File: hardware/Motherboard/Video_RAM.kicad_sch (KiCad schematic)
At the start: 59 parts, among them J1 DA15_Socket, J9 DIN-5_180degree, Q1 2N2222, Q2 2N2222, Q3 2N2222, Q4 2N2222, Q5 2N2222, Q6 2N2222, Q7 2N2222, U25 74LS74, U32 74LS04, U33 74LS17, U34 74LS166, U35 74LS166, U36 74LS166, U37 74LS166, U38 MK4116N, U39 MK4116N, U40 MK4116N, U41 MK4116N, U42 MK4116N, U43 MK4116N, U44 MK4116N, U45 MK4116N, U46 MK4116N, U47 MK4116N, U48 MK4116N, U49 MK4116N, U50 MK4116N, U51 MK4116N, U52 MK4116N, U53 MK4116N, U54 74LS374, U55 74LS374, U56 74LS541, U57 74LS32, U58 74LS374, U59 EF9365, U62 TBP18S030N, U63 74LS32, U64 74LS374

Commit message: WIP : passives parts, cosmetic stuffs.
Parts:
- added C43, C44, C45, C46, C47, C48, C49, C51, C52, C53, C54, C55, C56, C57, C58, C59, C60, C61, C62, C63, C64, C65, C66, C67, C68, C71: 100nF, symbol Device:C
- added R11, R5, R6: 1K, symbol Device:R
- renumbered J1 to J10
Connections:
- net TTL_B: now also R5.2
- net TTL_G: now also R6.2
- net TTL_R: now also R11.2
- net VCC12V: now also C51.1, C52.1, C53.1, C54.1
- net VCC5V: now also C43.1, C44.1, C45.1, C46.1, C47.1, C48.1, C49.1, C56.1, C58.1, C60.1, C62.1, C63.1, C64.1, C65.1, C66.1, C67.1, C68.1, C71.1, R11.1, R5.1, R6.1
- net VEE5V: now also C55.2, C57.2, C59.2, C61.2
- net VSS: now also C43.2, C44.2, C45.2, C46.2, C47.2, C48.2, C49.2, C51.2, C52.2, C53.2, C54.2, C55.1, C56.2, C57.1, C58.2, C59.1, C60.2, C61.1, C62.2, C63.2, C64.2, C65.2, C66.2, C67.2, C68.2, C71.2
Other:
- moved on the sheet: U32G, U33G, U57E, U63E

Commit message: Footprints.
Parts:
- C43, C44, C45, C46, C47, C48, C49, C51, C52, C53, C54, C55, C56, C57, C58, C59, C60, C61, C62, C63, C64, C65, C66, C67, C68, C71: footprint (none) -> Capacitor_THT:C_Disc_D9.0mm_W2.5mm_P5.00mm
- J10: footprint (none) -> Connector_Dsub:DSUB-15_Socket_Horizontal_P2.77x2.84mm_EdgePinOffset9.40mm
- J9: footprint (none) -> Connector_PinHeader_2.54mm:PinHeader_1x05_P2.54mm_Vertical
- R1, R10, R11, R12, R13, R14, R15, R16, R17, R18, R19, R2, R3, R4, R41, R46, R5, R6, R7, R8, R9: footprint (none) -> Resistor_THT:R_Axial_DIN0309_L9.0mm_D3.2mm_P12.70mm_Horizontal
- U25, U32, U33, U57, U63: footprint (none) -> Package_DIP:DIP-14_W7.62mm_Socket
- U34, U35, U36, U37, U62: footprint (none) -> Package_DIP:DIP-16_W7.62mm_Socket
- U38, U39, U40, U41, U42, U43, U44, U45, U46, U47, U48, U49, U50, U51, U52, U53: footprint Package_DIP:DIP-16_W7.62mm -> Package_DIP:DIP-16_W7.62mm_Socket
- U54, U55, U56, U58, U64: footprint (none) -> Package_DIP:DIP-20_W7.62mm_Socket
- U59: footprint Package_DIP:DIP-40_W15.24mm -> Package_DIP:DIP-40_W15.24mm_Socket

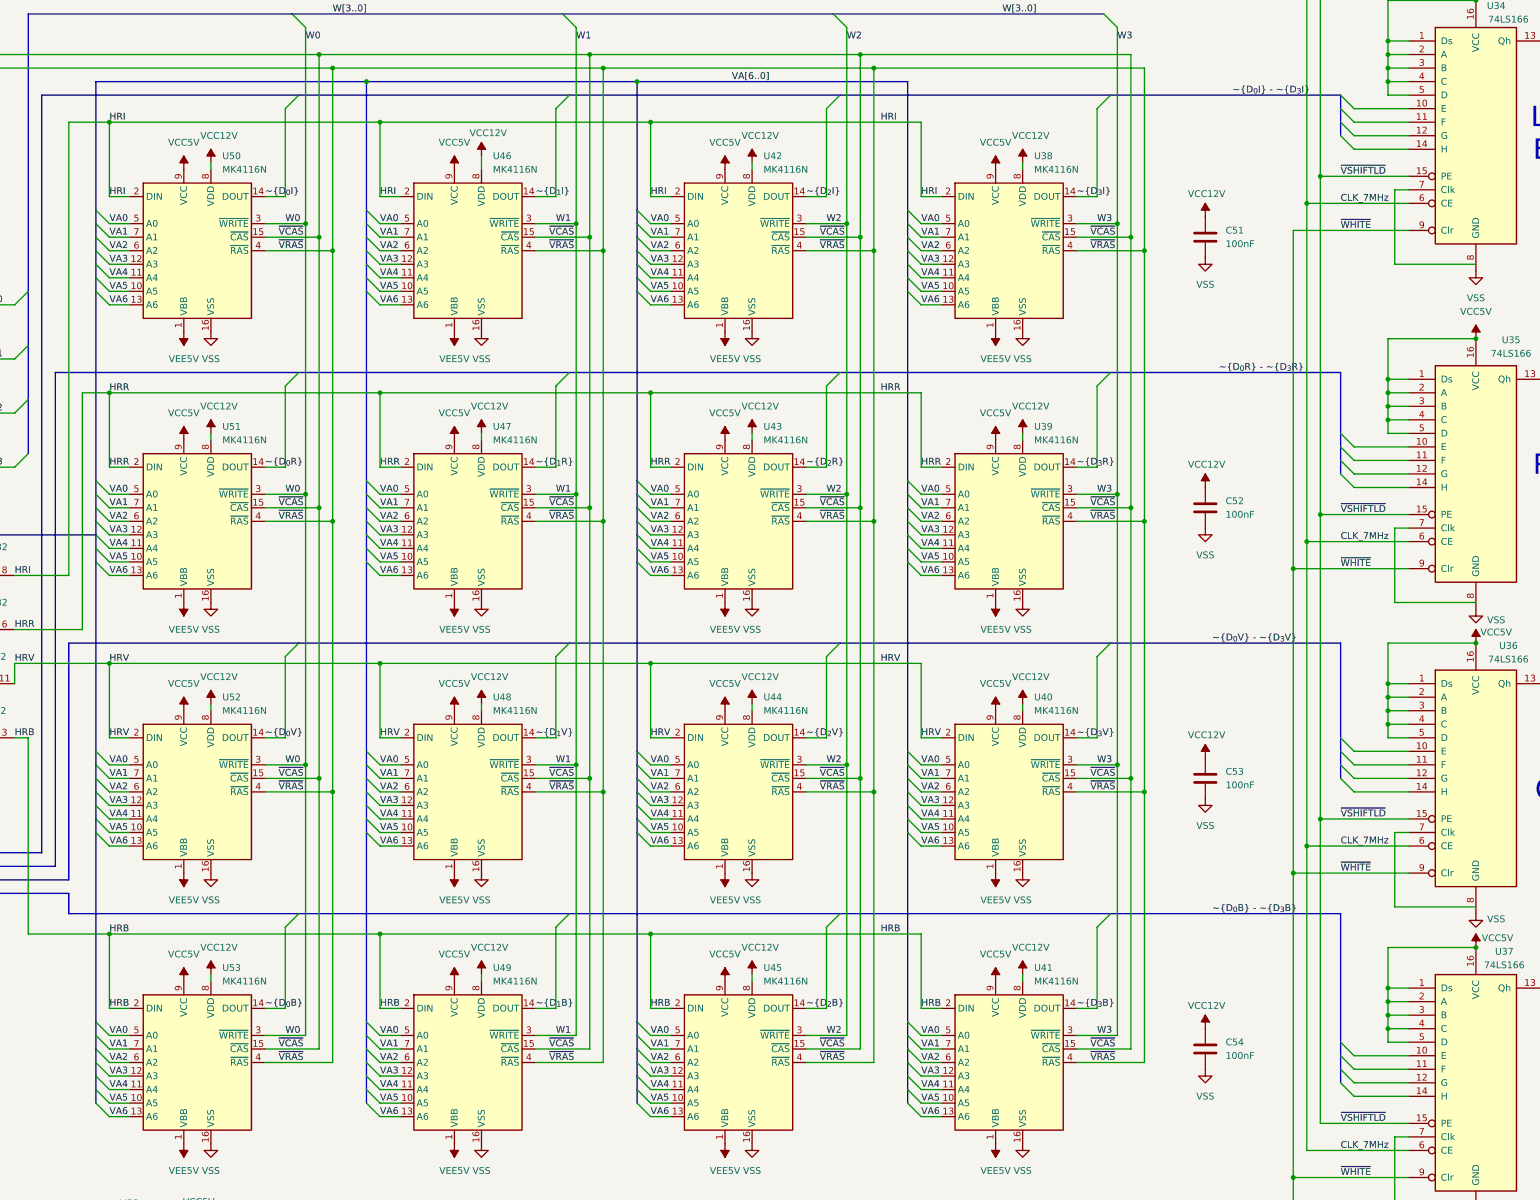
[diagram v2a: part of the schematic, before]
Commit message: fix dram address bit order.
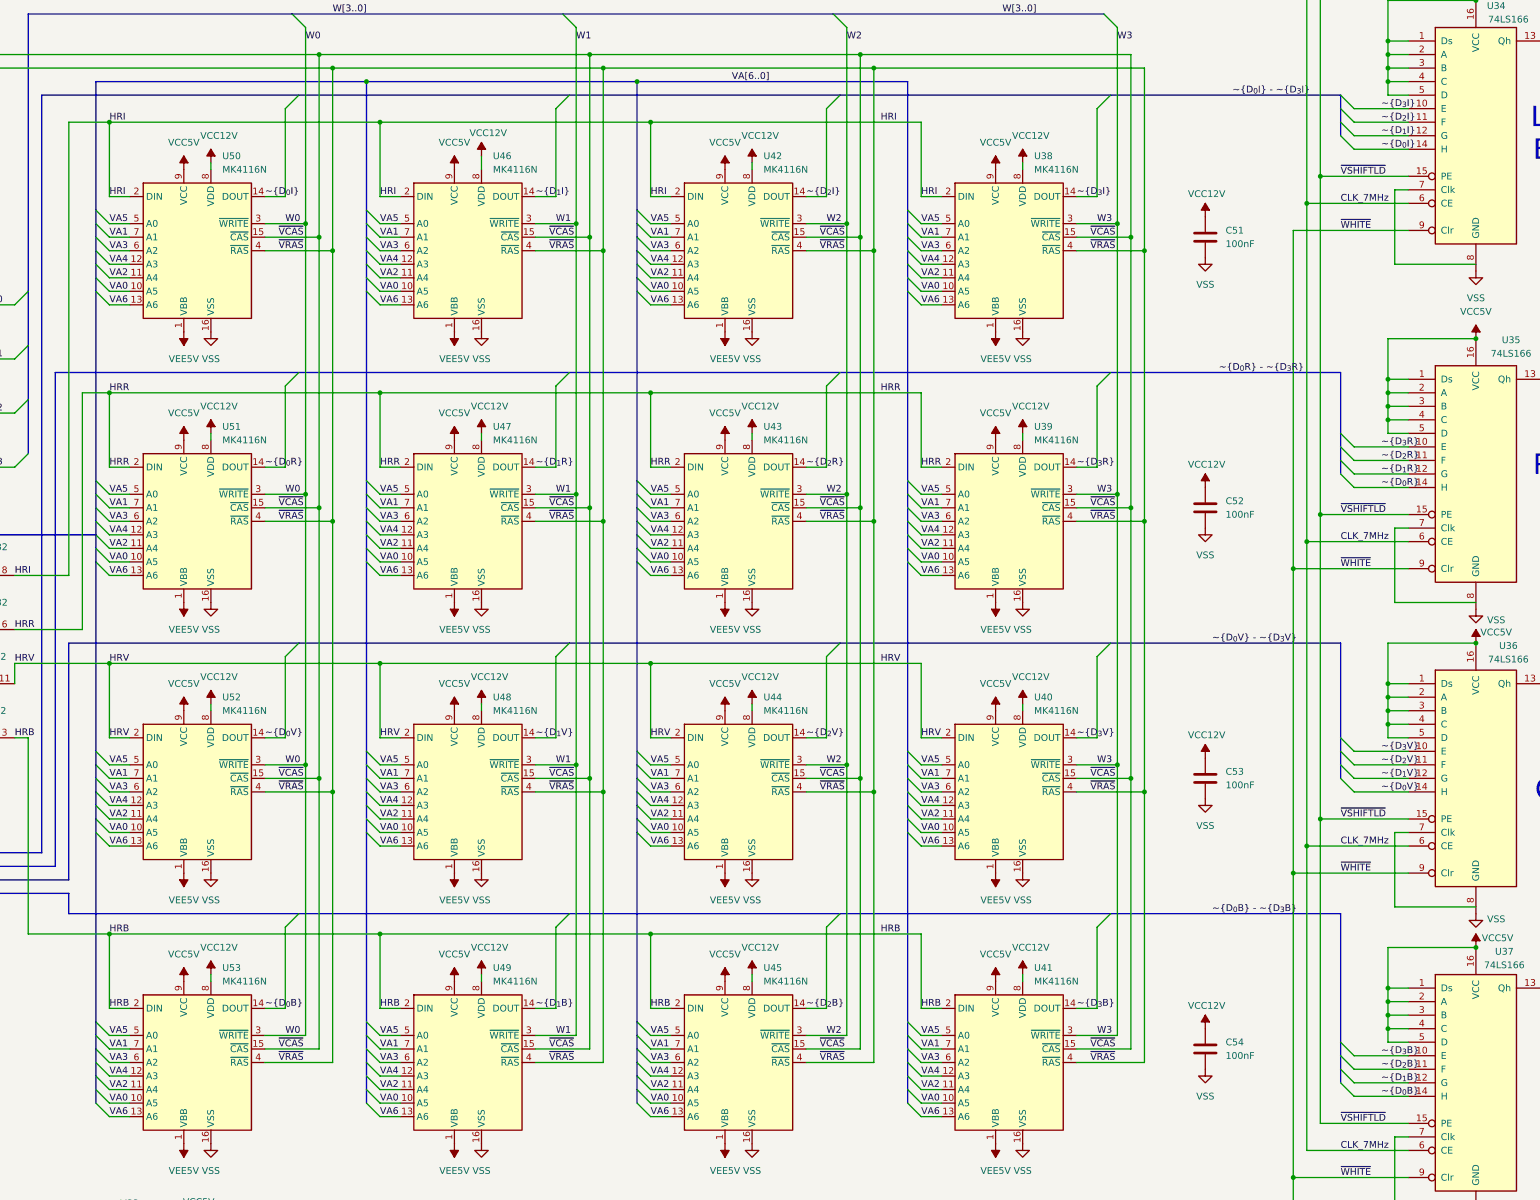
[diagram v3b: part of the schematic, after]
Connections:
- net VA0: now also U38.10 (A5), U39.10 (A5), U40.10 (A5), U41.10 (A5), U42.10 (A5), U43.10 (A5), U44.10 (A5), U45.10 (A5), U46.10 (A5), U47.10 (A5), U48.10 (A5), U49.10 (A5), U50.10 (A5), U51.10 (A5), U52.10 (A5), U53.10 (A5); no longer U38.5 (A0), U39.5 (A0), U40.5 (A0), U41.5 (A0), U42.5 (A0), U43.5 (A0), U44.5 (A0), U45.5 (A0), U46.5 (A0), U47.5 (A0), U48.5 (A0), U49.5 (A0), U50.5 (A0), U51.5 (A0), U52.5 (A0), U53.5 (A0)
- net VA2: now also U38.11 (A4), U39.11 (A4), U40.11 (A4), U41.11 (A4), U42.11 (A4), U43.11 (A4), U44.11 (A4), U45.11 (A4), U46.11 (A4), U47.11 (A4), U48.11 (A4), U49.11 (A4), U50.11 (A4), U51.11 (A4), U52.11 (A4), U53.11 (A4); no longer U38.6 (A2), U39.6 (A2), U40.6 (A2), U41.6 (A2), U42.6 (A2), U43.6 (A2), U44.6 (A2), U45.6 (A2), U46.6 (A2), U47.6 (A2), U48.6 (A2), U49.6 (A2), U50.6 (A2), U51.6 (A2), U52.6 (A2), U53.6 (A2)
- net VA3: now also U38.6 (A2), U39.6 (A2), U40.6 (A2), U41.6 (A2), U42.6 (A2), U43.6 (A2), U44.6 (A2), U45.6 (A2), U46.6 (A2), U47.6 (A2), U48.6 (A2), U49.6 (A2), U50.6 (A2), U51.6 (A2), U52.6 (A2), U53.6 (A2); no longer U38.12 (A3), U39.12 (A3), U40.12 (A3), U41.12 (A3), U42.12 (A3), U43.12 (A3), U44.12 (A3), U45.12 (A3), U46.12 (A3), U47.12 (A3), U48.12 (A3), U49.12 (A3), U50.12 (A3), U51.12 (A3), U52.12 (A3), U53.12 (A3)
- net VA4: now also U38.12 (A3), U39.12 (A3), U40.12 (A3), U41.12 (A3), U42.12 (A3), U43.12 (A3), U44.12 (A3), U45.12 (A3), U46.12 (A3), U47.12 (A3), U48.12 (A3), U49.12 (A3), U50.12 (A3), U51.12 (A3), U52.12 (A3), U53.12 (A3); no longer U38.11 (A4), U39.11 (A4), U40.11 (A4), U41.11 (A4), U42.11 (A4), U43.11 (A4), U44.11 (A4), U45.11 (A4), U46.11 (A4), U47.11 (A4), U48.11 (A4), U49.11 (A4), U50.11 (A4), U51.11 (A4), U52.11 (A4), U53.11 (A4)
- net VA5: now also U38.5 (A0), U39.5 (A0), U40.5 (A0), U41.5 (A0), U42.5 (A0), U43.5 (A0), U44.5 (A0), U45.5 (A0), U46.5 (A0), U47.5 (A0), U48.5 (A0), U49.5 (A0), U50.5 (A0), U51.5 (A0), U52.5 (A0), U53.5 (A0); no longer U38.10 (A5), U39.10 (A5), U40.10 (A5), U41.10 (A5), U42.10 (A5), U43.10 (A5), U44.10 (A5), U45.10 (A5), U46.10 (A5), U47.10 (A5), U48.10 (A5), U49.10 (A5), U50.10 (A5), U51.10 (A5), U52.10 (A5), U53.10 (A5)
- net ~{D_{0}B}: now also U37.14 (H)
- net ~{D_{0}I}: now also U34.14 (H)
- net ~{D_{0}R}: now also U35.14 (H)
- net ~{D_{0}V}: now also U36.14 (H)
- net ~{D_{1}B}: now also U37.12 (G)
- net ~{D_{1}I}: now also U34.12 (G)
- net ~{D_{1}R}: now also U35.12 (G)
- net ~{D_{1}V}: now also U36.12 (G)
- net ~{D_{2}B}: now also U37.11 (F)
- net ~{D_{2}I}: now also U34.11 (F)
- net ~{D_{2}R}: now also U35.11 (F)
- net ~{D_{2}V}: now also U36.11 (F)
- net ~{D_{3}B}: now also U37.10 (E)
- net ~{D_{3}I}: now also U34.10 (E)
- net ~{D_{3}R}: now also U35.10 (E)
- net ~{D_{3}V}: now also U36.10 (E)

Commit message: Connectors footprint.
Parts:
- J9: footprint Connector_PinHeader_2.54mm:PinHeader_1x05_P2.54mm_Vertical -> Library:DIN5-RA-PTH
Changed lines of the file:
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@@
 			)
 		)
-		(property "Footprint" "Connector_PinHeader_2.54mm:PinHeader_1x05_P2.54mm_Vertical"
+		(property "Footprint" "Library:DIN5-RA-PTH"
 			(at 548.64 327.66 0)
 			(effects

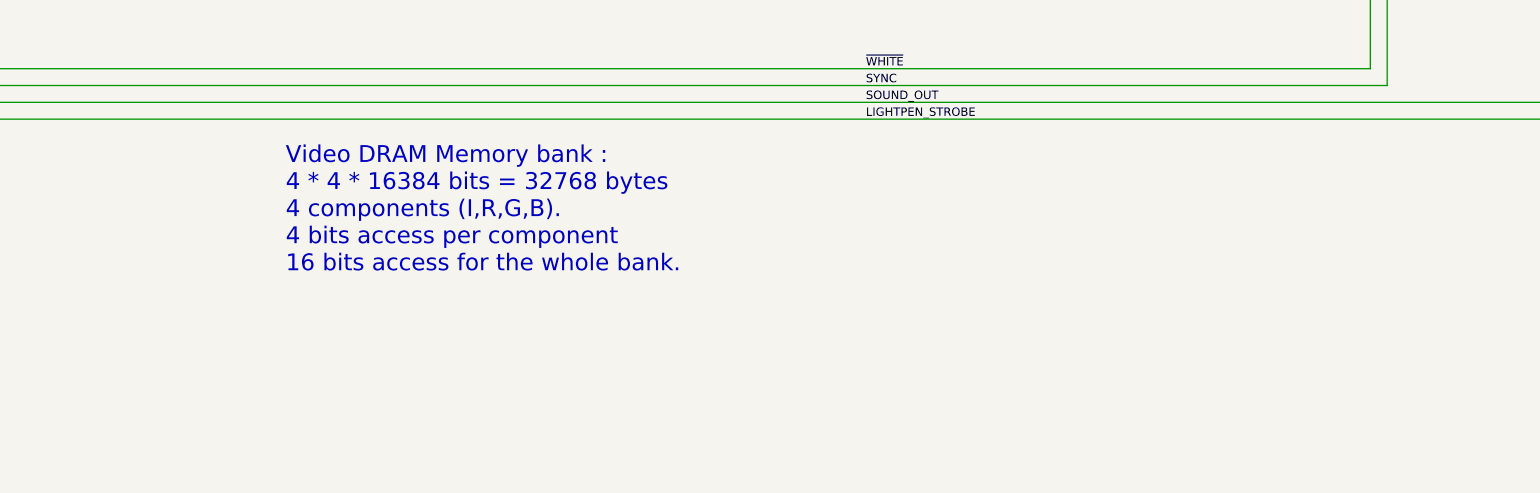
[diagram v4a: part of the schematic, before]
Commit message: add some descriptions / comments.
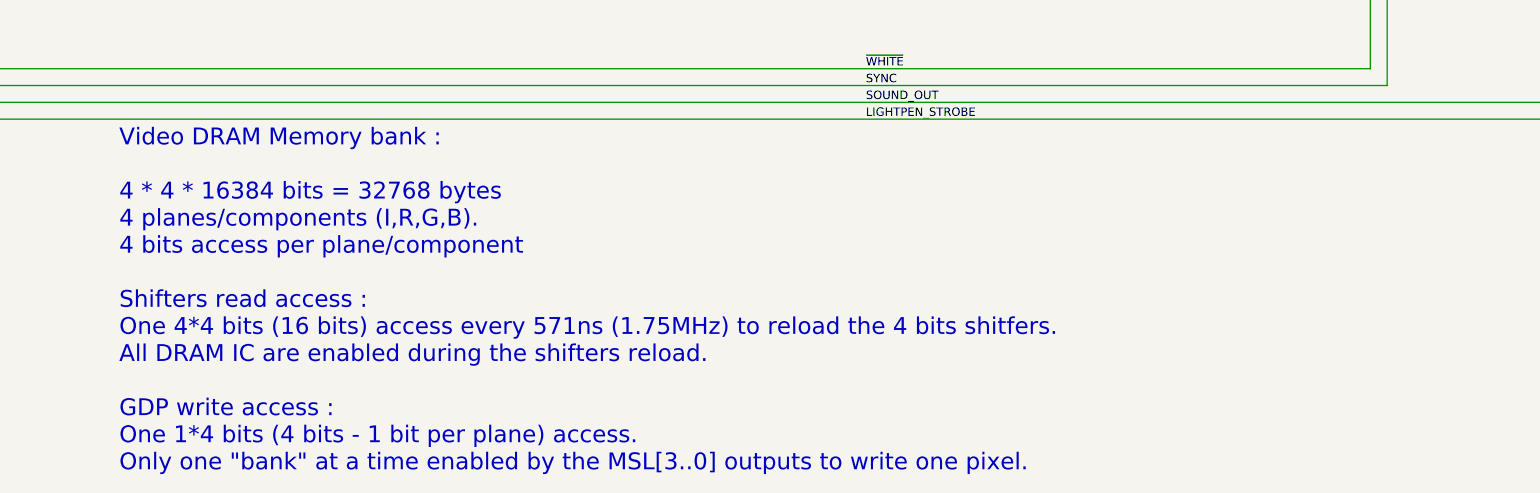
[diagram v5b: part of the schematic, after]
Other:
- note added: "Video DRAM Memory bank : 4 * 4 * 16384 bits = 32768 bytes 4 planes/components (I,R,G,B). 4 bits access per plane/component Shifters read access : One 4*4 bits (16 bits) access every 571ns (1.75MHz) to reload the 4 bits shitfers. All DRAM IC are enabled during the shifters reload. GDP write access : One 1*4 bits (4 bits - 1 bit per plane) access. Only one "bank" at a time enabled by the MSL[3..0] 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"
- note removed: "Video DRAM Memory bank : 4 * 4 * 16384 bits = 32768 bytes 4 components (I,R,G,B). 4 bits access per component 16 bits access for the whole bank."
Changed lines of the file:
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@@
 		)
 	)
-	(text "Video DRAM Memory bank :\n4 * 4 * 16384 bits = 32768 bytes\n4 components (I,R,G,B).\n4 bits access per component \n16 bits access for the whole bank. "
+	(text "Video DRAM Memory bank :\n\n4 * 4 * 16384 bits = 32768 bytes\n4 planes/components (I,R,G,B).\n4 bits access per plane/component\n\nShifters read access : \nOne 4*4 bits (16 bits) access every 571ns (1.75MHz) to reload the 4 bits shitfers. \nAll DRAM IC are enabled during the shifters reload.\n\nGDP write access :\nOne 1*4 bits (4 bits - 1 bit per plane) access.\nOnly one \"bank\" at a time enabled by the MSL[3..0] outputs to write one pixel.\n\n"
 		(exclude_from_sim no)
-		(at 261.62 327.406 0)
+		(at 236.474 343.154 0)
 		(effects
 			(font

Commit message: connection fix
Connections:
- net VSS: now also U34.7 (Clk), U35.7 (Clk), U36.7 (Clk), U37.7 (Clk)
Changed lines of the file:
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@@
 	)
 	(junction
+		(at 459.74 275.59)
+		(diameter 0)
+		(color 0 0 0 0)
+	)
+	(junction
 		(at 427.99 148.59)
 		(diameter 0)
@@
 	)
 	(junction
+		(at 459.74 161.29)
+		(diameter 0)
+		(color 0 0 0 0)
+	)
+	(junction
 		(at 397.51 144.78)
 		(diameter 0)
@@
 	)
 	(junction
+		(at 459.74 97.79)
+		(diameter 0)
+		(color 0 0 0 0)
+	)
+	(junction
 		(at 293.37 193.04)
 		(diameter 0)
@@
 	)
 	(junction
+		(at 459.74 218.44)
+		(diameter 0)
+		(color 0 0 0 0)
+	)
+	(junction
 		(at 344.17 57.15)
 		(diameter 0)
@@
 	(wire
 		(pts
+			(xy 459.74 97.79) (xy 444.5 97.79)
+		)
+		(stroke
+			(width 0)
+			(type default)
+		)
+	)
+	(wire
+		(pts
 			(xy 384.81 93.98) (xy 397.51 93.98)
 		)
@@
 	(wire
 		(pts
-			(xy 444.5 274.32) (xy 444.5 260.35)
-		)
-		(stroke
-			(width 0)
-			(type default)
-		)
-	)
-	(wire
-		(pts
 			(xy 436.88 138.43) (xy 447.04 138.43)
 		)
@@
 	(wire
 		(pts
+			(xy 459.74 161.29) (xy 444.5 161.29)
+		)
+		(stroke
+			(width 0)
+			(type default)
+		)
+	)
+	(wire
+		(pts
 			(xy 384.81 91.44) (xy 394.97 91.44)
 		)
@@
 	(wire
 		(pts
-			(xy 444.5 160.02) (xy 444.5 146.05)
+			(xy 444.5 146.05) (xy 444.5 161.29)
 		)
 		(stroke
@@
 		)
 	)
+	(wire
+		(pts
+			(xy 459.74 275.59) (xy 444.5 275.59)
+		)
+		(stroke
+			(width 0)
+			(type default)
+		)
+	)
 	(bus
 		(pts
@@
 	(wire
 		(pts
-			(xy 459.74 274.32) (xy 444.5 274.32)
-		)
-		(stroke
-			(width 0)
-			(type default)
-		)
-	)
-	(wire
-		(pts
 			(xy 384.81 195.58) (xy 397.51 195.58)
 		)
@@
 	(wire
 		(pts
-			(xy 444.5 96.52) (xy 444.5 82.55)
+			(xy 444.5 82.55) (xy 444.5 97.79)
 		)
 		(stroke
@@
 	(wire
 		(pts
+			(xy 444.5 260.35) (xy 444.5 275.59)
+		)
+		(stroke
+			(width 0)
+			(type default)
+		)
+	)
+	(wire
+		(pts
 			(xy 45.72 154.94) (xy 62.23 154.94)
 		)
@@
 		)
 	)
-	(wire
-		(pts
-			(xy 459.74 160.02) (xy 444.5 160.02)
-		)
-		(stroke
-			(width 0)
-			(type default)
-		)
-	)
 	(bus
 		(pts
@@
 	(wire
 		(pts
+			(xy 459.74 218.44) (xy 444.5 218.44)
+		)
+		(stroke
+			(width 0)
+			(type default)
+		)
+	)
+	(wire
+		(pts
 			(xy 48.26 96.52) (xy 48.26 64.77)
 		)
@@
 	(wire
 		(pts
+			(xy 444.5 203.2) (xy 444.5 218.44)
+		)
+		(stroke
+			(width 0)
+			(type default)
+		)
+	)
+	(wire
+		(pts
 			(xy 511.81 293.37) (xy 511.81 294.64)
 		)
@@
 	(wire
 		(pts
-			(xy 459.74 217.17) (xy 444.5 217.17)
-		)
-		(stroke
-			(width 0)
-			(type default)
-		)
-	)
-	(wire
-		(pts
 			(xy 511.81 190.5) (xy 511.81 191.77)
 		)
@@
 		)
 	)
-	(wire
-		(pts
-			(xy 444.5 217.17) (xy 444.5 203.2)
-		)
-		(stroke
-			(width 0)
-			(type default)
-		)
-	)
 	(bus
 		(pts
@@
 		)
 		(stroke
-			(width 0)
-			(type default)
-		)
-	)
-	(wire
-		(pts
-			(xy 459.74 96.52) (xy 444.5 96.52)
-		)
-		(stroke
